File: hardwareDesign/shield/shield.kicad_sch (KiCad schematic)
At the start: 3 parts, among them J1 40_POS_RIBBON, J2 40_POS_Header

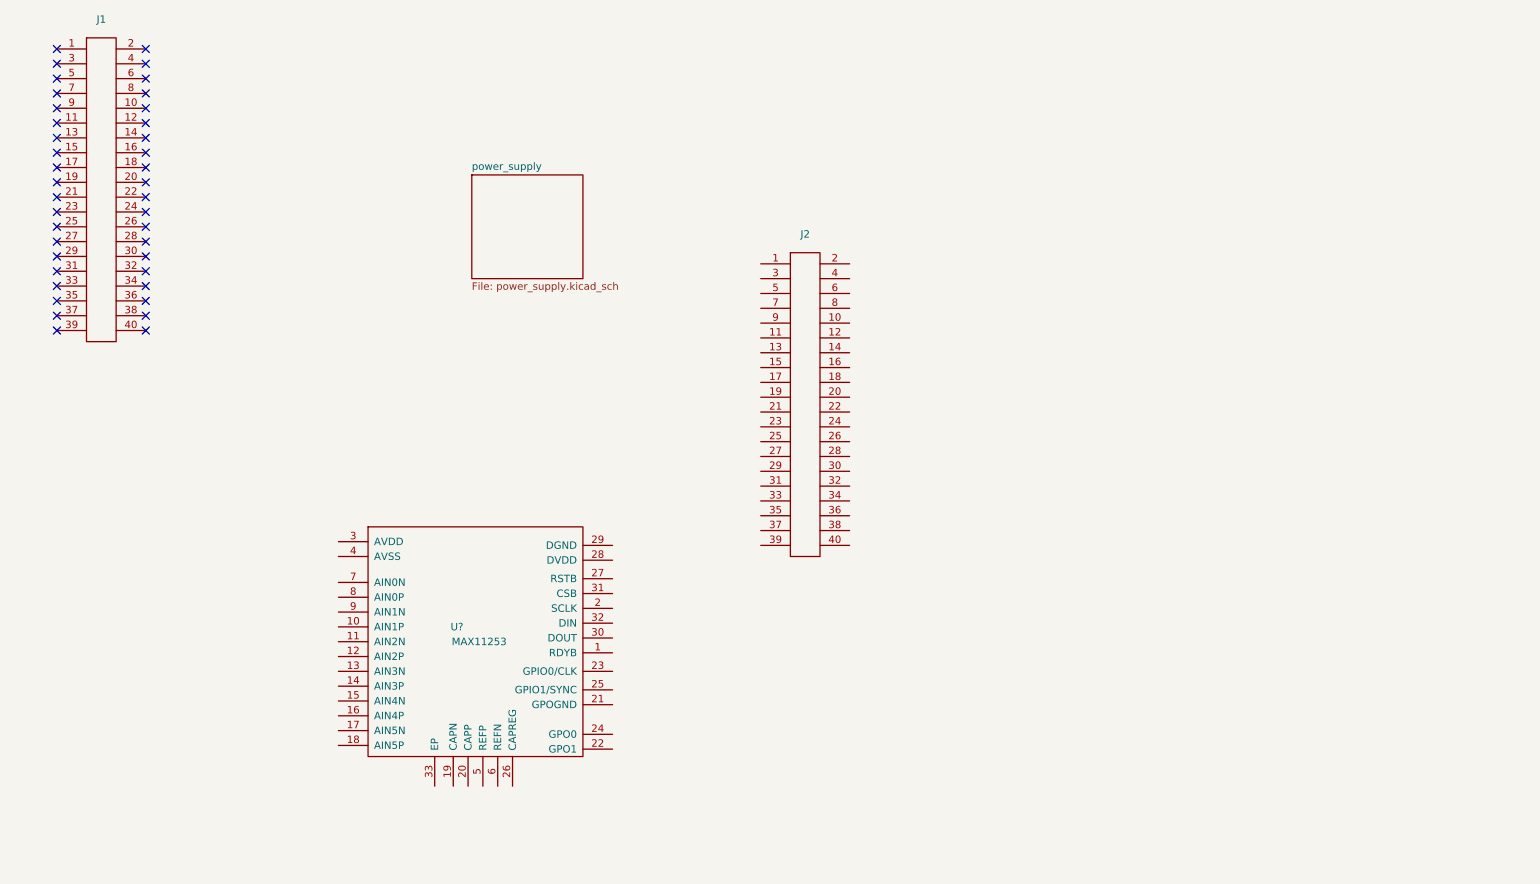
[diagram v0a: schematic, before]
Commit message: Schematic done
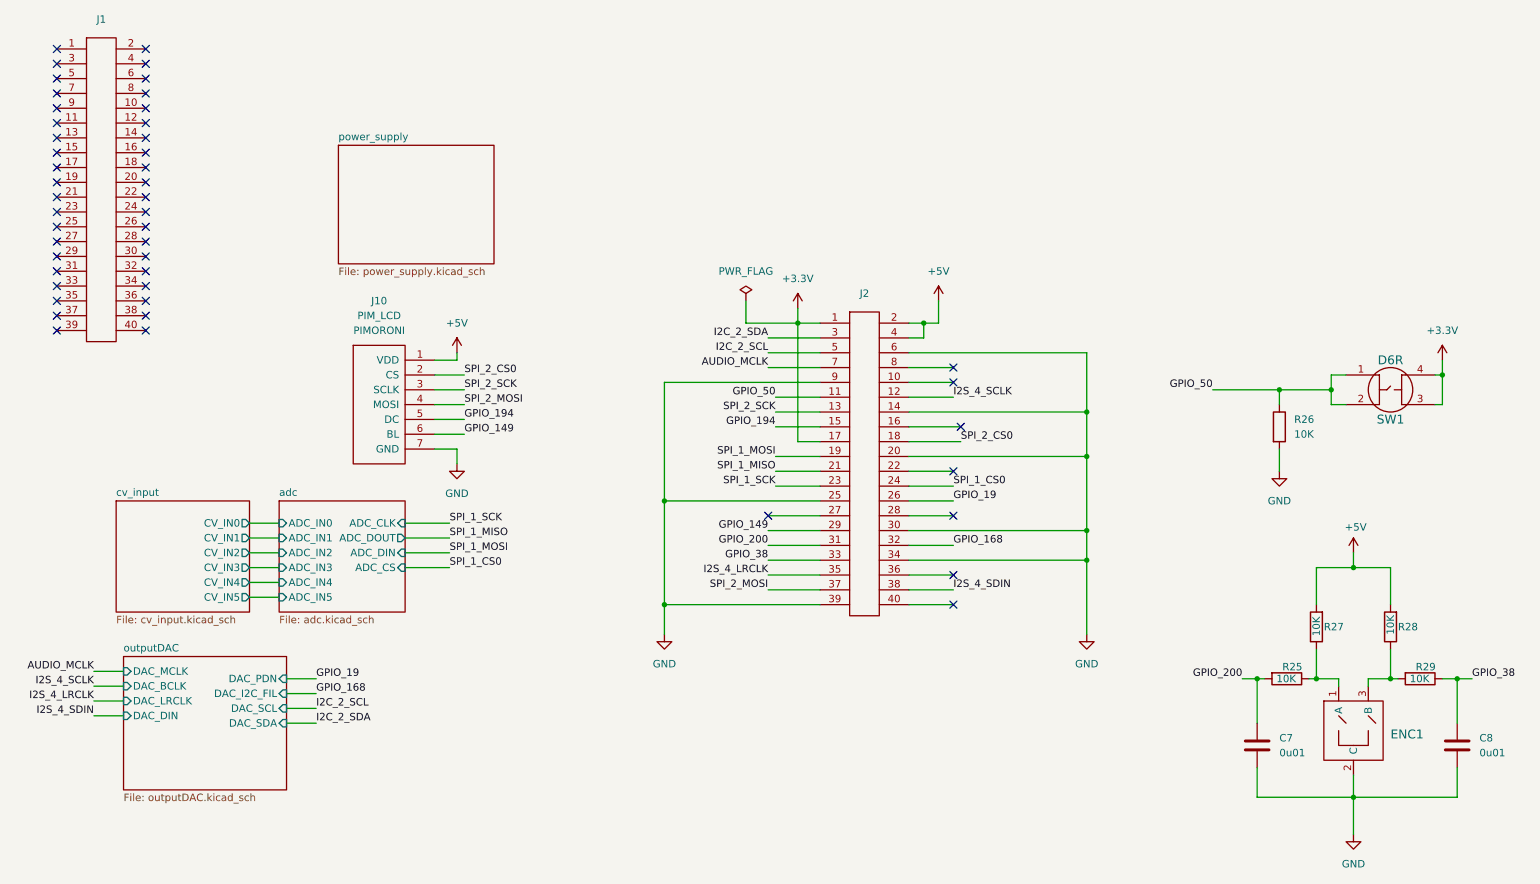
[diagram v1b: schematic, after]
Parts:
- removed U?: MAX11253, codecs:TQFN-32_EP_5x5, symbol codecs:MAX11253
- added C7, C8: 0.01uf_0603_50V, capacitors:SMD_0603[1608], symbol capacitors_smd:0.01uf_0603_50V
- added ENC1: BOURNS_PEC11R_DET, encoders:BOURNS_ENCODER, symbol encoders:BOURNS_PEC11R_DET
- added J10: PIM_LCD, display:PIMORONI_LCD_240x240, symbol display:PIM_LCD
- added R25, R27, R28, R29: 10K_0603_2, resistors:SMD_0603[1608], symbol resistors_smd:10K_0603_2
- added R26: 10K_0603, resistors:SMD_0603[1608], symbol resistors_smd:10K_0603
- added SW1: D6R, switches:D6R, symbol switches:D6R
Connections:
- net +3V3: now reaches J2.1
- net +3V3: now also J2.17, SW1.3, SW1.4
- net GPIO_50: now reaches J2.11
- net GPIO_50: now also R26.1, SW1.1, SW1.2
- net I2S_4_SCLK: now reaches J2.12
- net SPI_2_SCK: now reaches J2.13
- net SPI_2_SCK: now also J10.3 (SCLK)
- net GND: now reaches J2.14
- net GND: now also J2.20, J2.25, J2.30, J2.34, J2.39, J2.6, J2.9, C7.2, C8.2, ENC1.2 (C), J10.7 (GND), R26.2
- net GPIO_194: now reaches J2.15
- net GPIO_194: now also J10.5 (DC)
- net SPI_2_CS0: now reaches J2.18
- net SPI_2_CS0: now also J10.2 (CS)
- net SPI_1_MOSI: now reaches J2.19
- net +5V: now reaches J2.2
- net +5V: now also J2.4, J10.1 (VDD), R27.2, R28.2
- net SPI_1_MISO: now reaches J2.21
- net SPI_1_SCK: now reaches J2.23
- net SPI_1_CS0: now reaches J2.24
- net GPIO_19: now reaches J2.26
- net GPIO_149: now reaches J2.29
- net GPIO_149: now also J10.6 (BL)
- net I2C_2_SDA: now reaches J2.3
- net GPIO_200: now reaches J2.31
- net GPIO_200: now also C7.1, R25.2
- net GPIO_168: now reaches J2.32
- net GPIO_38: now reaches J2.33
- net GPIO_38: now also C8.1, R29.1
- net I2S_4_LRCLK: now reaches J2.35
- net SPI_2_MOSI: now reaches J2.37
- net SPI_2_MOSI: now also J10.4 (MOSI)
- net I2S_4_SDIN: now reaches J2.38
- net I2C_2_SCL: now reaches J2.5
- net AUDIO_MCLK: now reaches J2.7
- new net: ENC1.3 (B), R28.1, R29.2
- new net: ENC1.1 (A), R25.1, R27.1
- no-connect marks 40 -> 48
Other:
- added sheet adc (adc.kicad_sch)
- added sheet cv_input (cv_input.kicad_sch)
- added sheet outputDAC (outputDAC.kicad_sch)
- moved on the sheet: J2

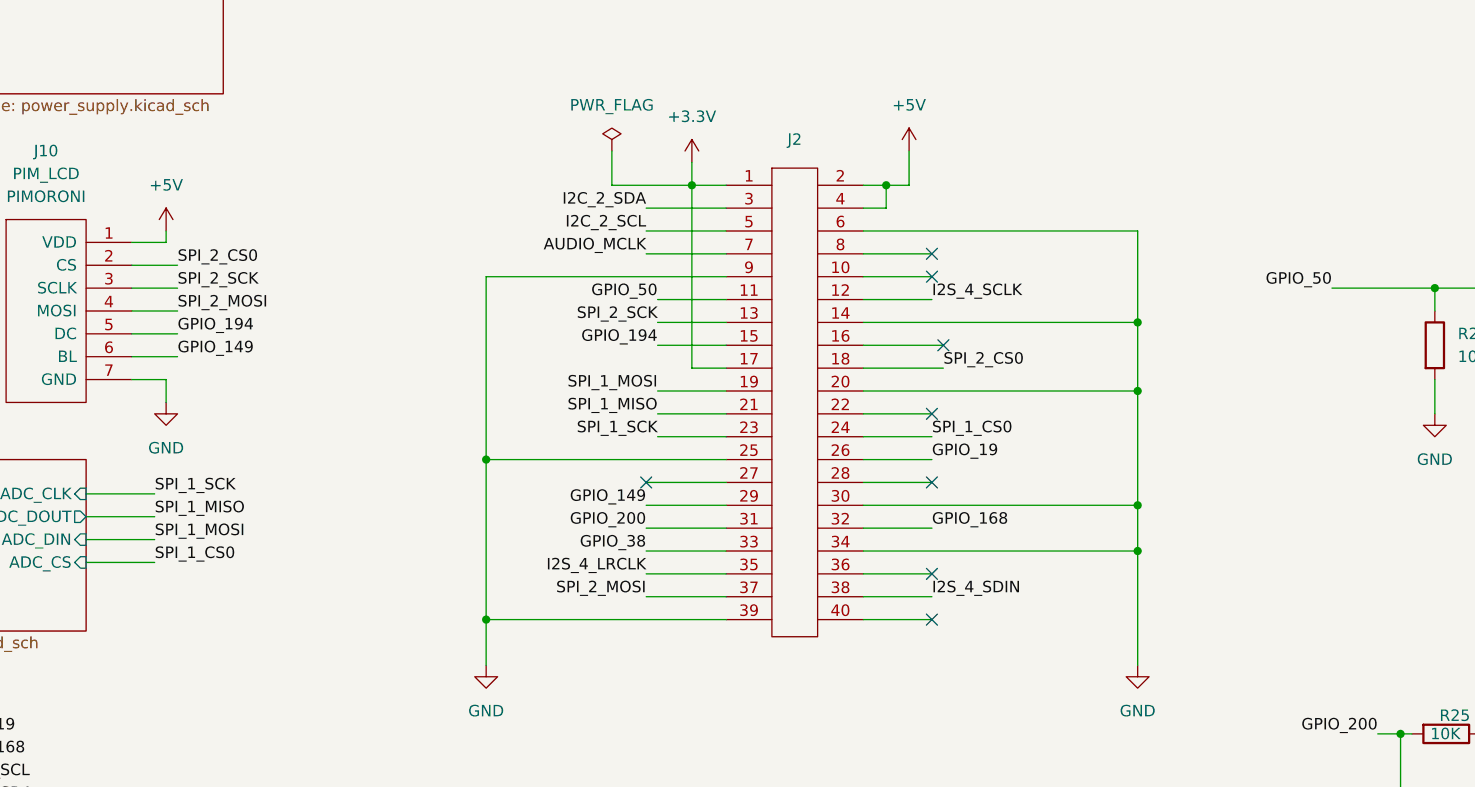
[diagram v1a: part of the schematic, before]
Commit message: Finished schematic and PCB for jetson Nano Sheild
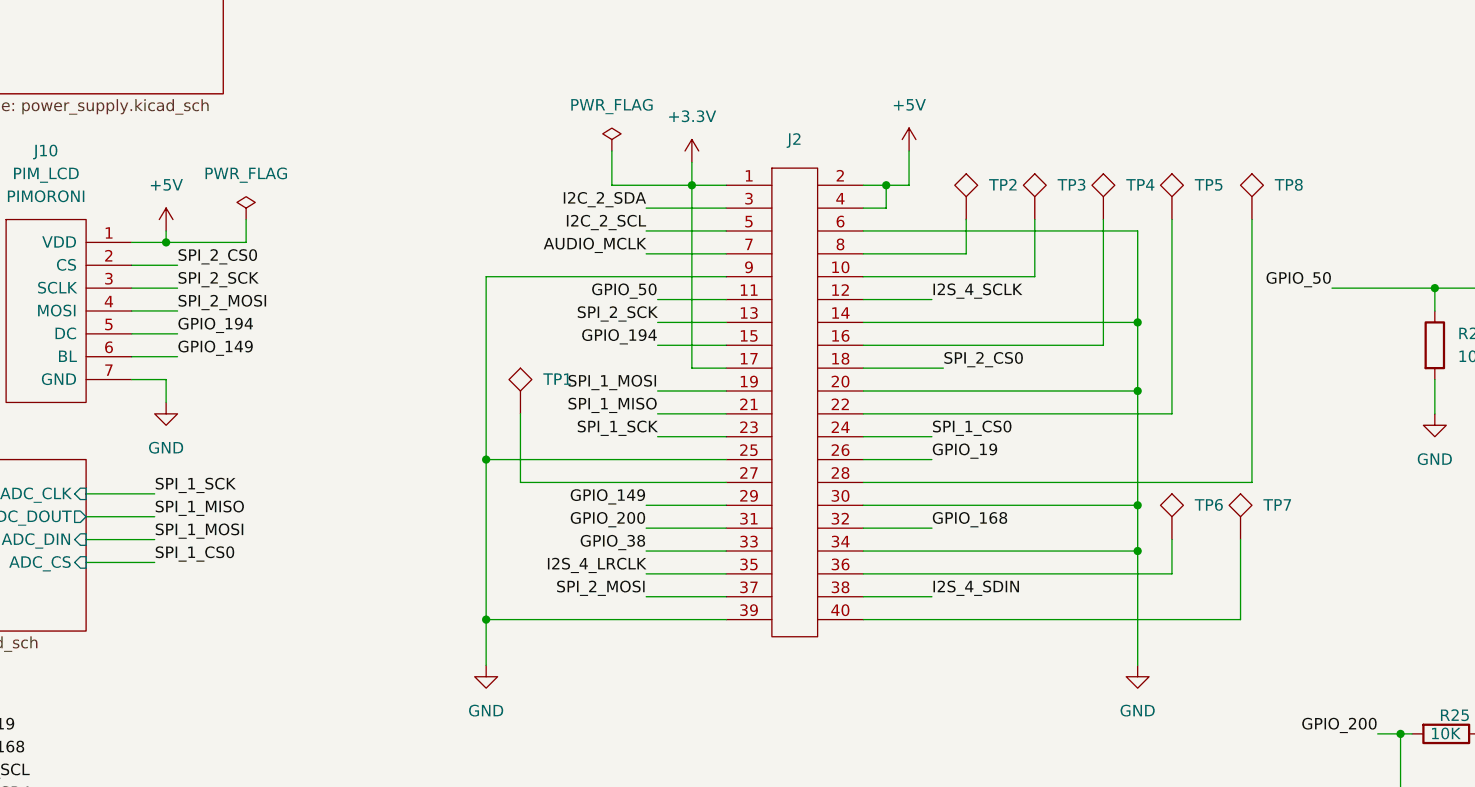
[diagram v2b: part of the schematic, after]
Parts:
- added TP1, TP2, TP3, TP4, TP5, TP6, TP7, TP8: test_point_TH_Small, misc:test_point_0.6mm, symbol test_points:test_point_TH_Small
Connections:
- net at J2.10: now also TP3.1
- net at J2.16: now also TP4.1
- net at J2.22: now also TP5.1
- net at J2.27: now also TP1.1
- net at J2.28: now also TP8.1
- net at J2.36: now also TP6.1
- net at J2.40: now also TP7.1
- net at J2.8: now also TP2.1
- no-connect marks 48 -> 40

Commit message: Finished layout with JN real footprint
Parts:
- added JN1: JetsonNano, singleBoardComp:jetsonNanoDev, symbol singleBoardComputers:JetsonNano
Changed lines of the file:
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@@
     (pin "2")
+  )
+  (symbol (lib_id "singleBoardComputers:JetsonNano") (at 162.56 31.75 0) (unit 1)
+    (in_bom yes) (on_board yes) (fields_autoplaced)
+    (property "Reference" "JN1" (id 0) (at 166.37 30.4799 0)
+      (effects (font (size 1.27 1.27)) (justify left))
+    )
+    (property "Value" "JetsonNano" (id 1) (at 163.068 42.291 0)
+      (effects (font (size 1.27 1.27)) hide)
+    )
+    (property "Footprint" "singleBoardComp:jetsonNanoDev" (id 2) (at 162.306 37.338 0)
+      (effects (font (size 1.27 1.27)) hide)
+    )
+    (property "Datasheet" "https://developer.nvidia.com/embedded/jetson-nano-developer-kit" (id 3) (at 164.846 48.26 0)
+      (effects (font (size 1.27 1.27)) hide)
+    )
+    (property "Manufacturer" "NVidia" (id 4) (at 162.687 44.958 0)
+      (effects (font (size 1.27 1.27)) hide)
+    )
+    (property "Part Number" "RCG04021K00FKED" (id 5) (at 162.433 39.878 0)
+      (effects (font (size 1.524 1.524)) hide)
+    )
+    (property "Display" "JetsonNanoDevKit" (id 6) (at 166.37 33.0199 0)
+      (effects (font (size 1.27 1.27)) (justify left))
+    )
+    (property "IPN" "SBC-001-000" (id 7) (at 161.925 27.305 0)
+      (effects (font (size 1.27 1.27)) hide)
+    )
   )
   (symbol (lib_id "power:+5V") (at 91.44 71.12 0) (unit 1)
@@
       (reference "J15") (unit 1) (value "2x1_PIN_HEADER") (footprint "connectors:02x01_2.54_pitch_pin_header")
     )
+    (path "/2a76dbce-1f6a-4d0c-b8f0-4094f860c076"
+      (reference "JN1") (unit 1) (value "JetsonNano") (footprint "singleBoardComp:jetsonNanoDev")
+    )
     (path "/125194e1-2af1-4944-8919-ee08a5925fe8/cc6fab20-8270-45c7-843f-e99bdf02d74d"
